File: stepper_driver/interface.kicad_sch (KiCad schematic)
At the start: 16 parts, among them J1 Conn_FFC_20_Pin_1mm_bottom-ZF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, J2 Conn_TERM_HDR_01x08_Pin_3.5MM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, U1 LVDS_4-4_HALF_DS91M040TSQE, U2 LVDS_4-4_HALF_DS91M040TSQE, U2 MAX6817

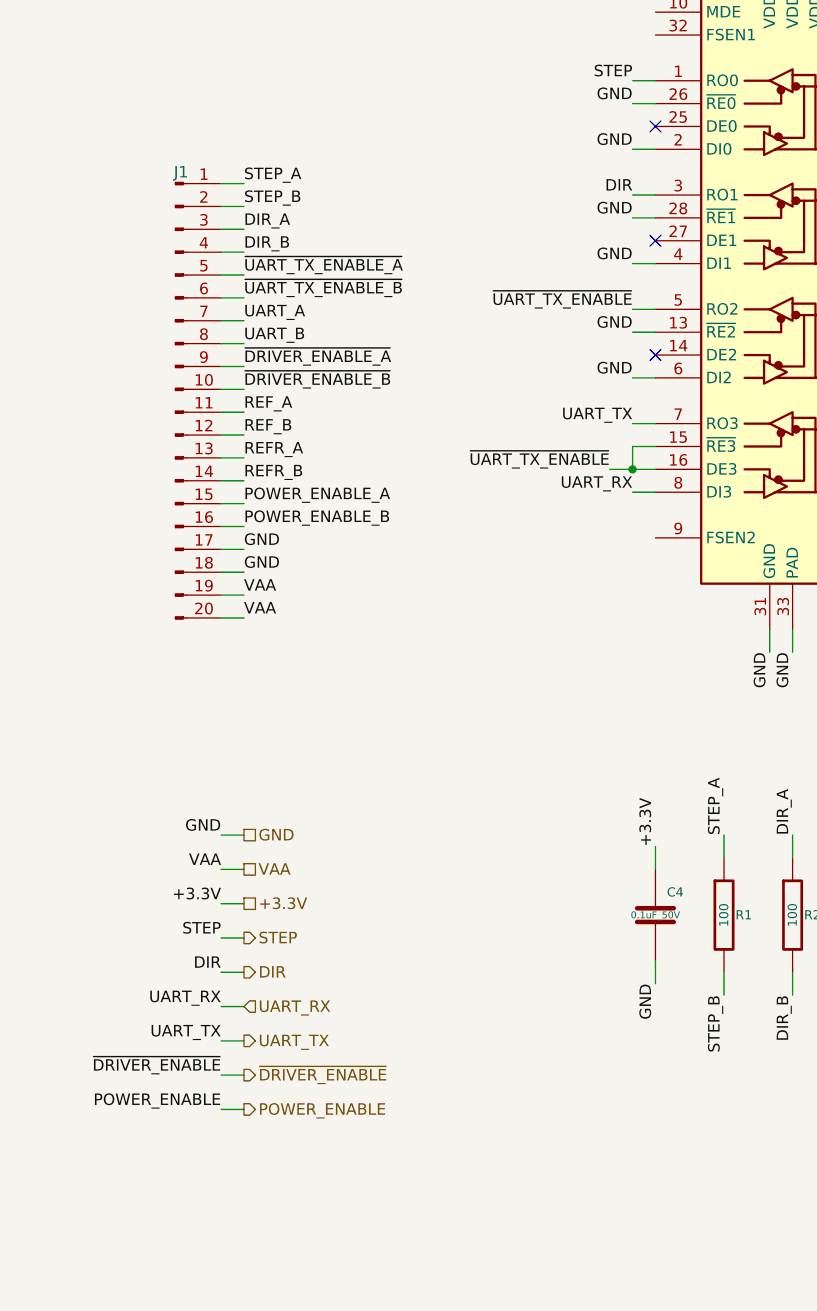
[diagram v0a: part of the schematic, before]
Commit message: Rearrange some wiring
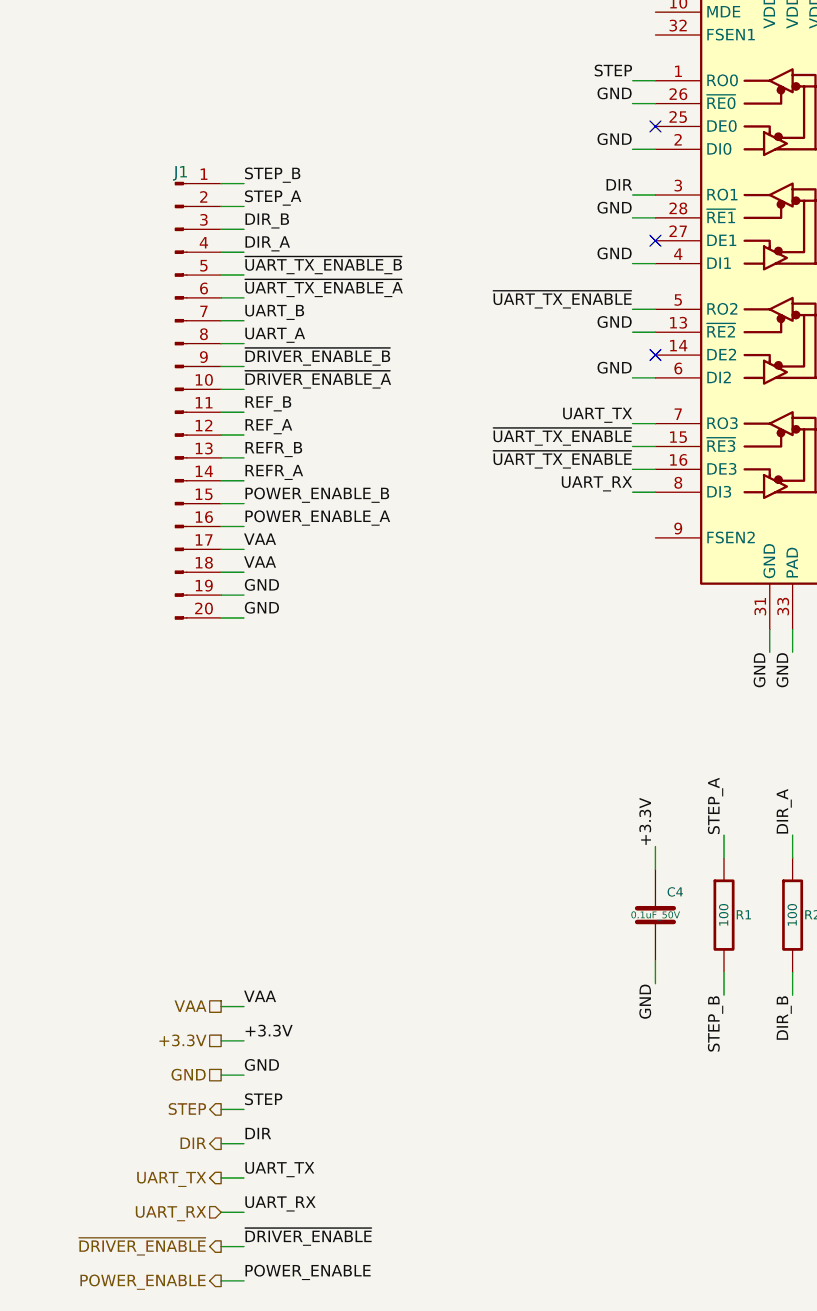
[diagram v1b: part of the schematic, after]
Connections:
- net DIR_A: now also J1.4 (Pin_4); no longer J1.3 (Pin_3)
- net DIR_B: now also J1.3 (Pin_3); no longer J1.4 (Pin_4)
- net GND: now also J1.19 (Pin_19), J1.20 (Pin_20); no longer J1.17 (Pin_17), J1.18 (Pin_18)
- net POWER_ENABLE_A: now also J1.16 (Pin_16); no longer J1.15 (Pin_15)
- net POWER_ENABLE_B: now also J1.15 (Pin_15); no longer J1.16 (Pin_16)
- net REFR_A: now also J1.14 (Pin_14); no longer J1.13 (Pin_13)
- net REFR_B: now also J1.13 (Pin_13); no longer J1.14 (Pin_14)
- net REF_A: now also J1.12 (Pin_12); no longer J1.11 (Pin_11)
- net REF_B: now also J1.11 (Pin_11); no longer J1.12 (Pin_12)
- net STEP_A: now also J1.2 (Pin_2); no longer J1.1 (Pin_1)
- net STEP_B: now also J1.1 (Pin_1); no longer J1.2 (Pin_2)
- net UART_A: now also J1.8 (Pin_8); no longer J1.7 (Pin_7)
- net UART_B: now also J1.7 (Pin_7); no longer J1.8 (Pin_8)
- net VAA: now also J1.17 (Pin_17), J1.18 (Pin_18); no longer J1.19 (Pin_19), J1.20 (Pin_20)
- net ~{DRIVER_ENABLE_A}: now also J1.10 (Pin_10); no longer J1.9 (Pin_9)
- net ~{DRIVER_ENABLE_B}: now also J1.9 (Pin_9); no longer J1.10 (Pin_10)
- net ~{UART_TX_ENABLE_A}: now also J1.6 (Pin_6); no longer J1.5 (Pin_5)
- net ~{UART_TX_ENABLE_B}: now also J1.5 (Pin_5); no longer J1.6 (Pin_6)

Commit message: Update
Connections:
- net +3.3V: now also U1.10 (MDE), U2.10 (MDE)
- no-connect marks 9 -> 13
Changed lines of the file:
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@@
   (title_block
     (title "stepper_driver")
-    (date "2023-05-16")
+    (date "2023-05-17")
     (rev "2.0")
     (company "Howard Hughes Medical Institute")
@@
   (no_connect (at 87.63 73.66))
   (no_connect (at 87.63 48.26))
+  (no_connect (at 87.63 38.1))
   (no_connect (at 167.64 58.42))
   (no_connect (at 167.64 55.88))
+  (no_connect (at 167.64 38.1))
+  (no_connect (at 87.63 93.98))
   (no_connect (at 167.64 71.12))
+  (no_connect (at 167.64 93.98))
   (no_connect (at 167.64 86.36))
   (wire (pts (xy 41.91 168.91) (xy 39.37 168.91))
@@
     (stroke (width 0) (type default))
   )
+  (wire (pts (xy 167.64 35.56) (xy 165.1 35.56))
+    (stroke (width 0) (type default))
+  )
   (wire (pts (xy 167.64 45.72) (xy 165.1 45.72))
     (stroke (width 0) (type default))
@@
     (stroke (width 0) (type default))
   )
+  (wire (pts (xy 87.63 35.56) (xy 85.09 35.56))
+    (stroke (width 0) (type default))
+  )
   (wire (pts (xy 180.34 27.94) (xy 180.34 25.4))
     (stroke (width 0) (type default))
@@
     (effects (font (size 1.27 1.27)) (justify left bottom))
   )
+  (label "+3.3V" (at 85.09 35.56 180) (fields_autoplaced)
+    (effects (font (size 1.27 1.27)) (justify right bottom))
+  )
   (label "GND" (at 167.64 143.51 270) (fields_autoplaced)
     (effects (font (size 1.27 1.27)) (justify right bottom))
@@
     (effects (font (size 1.27 1.27)) (justify right bottom))
   )
+  (label "+3.3V" (at 165.1 35.56 180) (fields_autoplaced)
+    (effects (font (size 1.27 1.27)) (justify right bottom))
+  )
